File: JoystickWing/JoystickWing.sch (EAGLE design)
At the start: 19 parts, among them J1 5747844-4

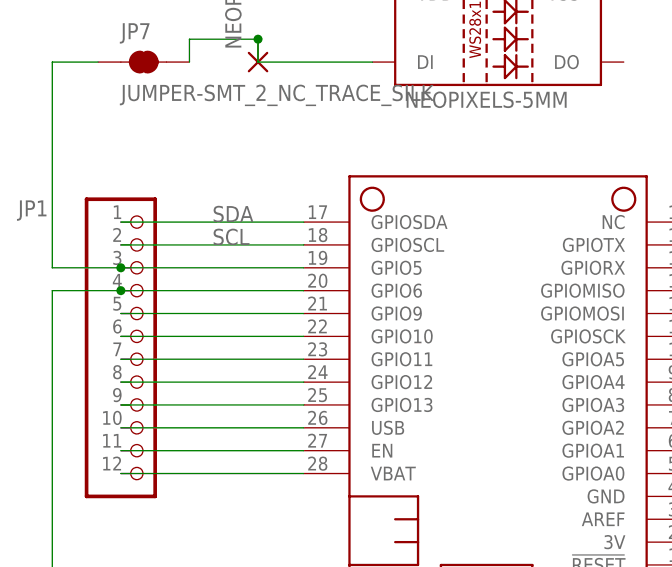
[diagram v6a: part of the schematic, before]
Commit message: Updated to fix errors and sent to PCBWay
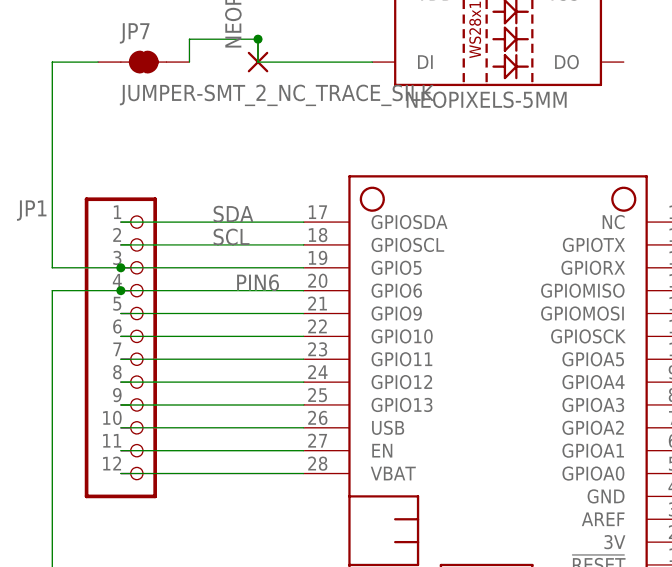
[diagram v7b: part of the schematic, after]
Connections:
- net N$2 renamed PIN6
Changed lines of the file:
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@@
 <grid distance="0.1" unitdist="inch" unit="inch" style="lines" multiple="1" display="no" altdistance="0.01" altunitdist="inch" altunit="inch"/>
 <layers>
-<layer number="1" name="Top" color="4" fill="1" visible="yes" active="no"/>
-<layer number="2" name="Route2" color="1" fill="3" visible="yes" active="no"/>
-<layer number="3" name="Route3" color="4" fill="3" visible="yes" active="no"/>
-<layer number="4" name="Route4" color="1" fill="4" visible="yes" active="no"/>
-<layer number="5" name="Route5" color="4" fill="4" visible="yes" active="no"/>
-<layer number="6" name="Route6" color="1" fill="8" visible="yes" active="no"/>
-<layer number="7" name="Route7" color="4" fill="8" visible="yes" active="no"/>
-<layer number="8" name="Route8" color="1" fill="2" visible="yes" active="no"/>
-<layer number="9" name="Route9" color="4" fill="2" visible="yes" active="no"/>
-<layer number="10" name="Route10" color="1" fill="7" visible="yes" active="no"/>
-<layer number="11" name="Route11" color="4" fill="7" visible="yes" active="no"/>
-<layer number="12" name="Route12" color="1" fill="5" visible="yes" active="no"/>
-<layer number="13" name="Route13" color="4" fill="5" visible="yes" active="no"/>
-<layer number="14" name="Route14" color="1" fill="6" visible="yes" active="no"/>
-<layer number="15" name="Route15" color="4" fill="6" visible="yes" active="no"/>
-<layer number="16" name="Bottom" color="1" fill="1" visible="yes" active="no"/>
-<layer number="17" name="Pads" color="2" fill="1" visible="yes" active="no"/>
-<layer number="18" name="Vias" color="2" fill="1" visible="yes" active="no"/>
-<layer number="19" name="Unrouted" color="6" fill="1" visible="yes" active="no"/>
-<layer number="20" name="Dimension" color="24" fill="1" visible="yes" active="no"/>
-<layer number="21" name="tPlace" color="7" fill="1" visible="yes" active="no"/>
-<layer number="22" name="bPlace" color="7" fill="1" visible="yes" active="no"/>
-<layer number="23" name="tOrigins" color="15" fill="1" visible="yes" active="no"/>
-<layer number="24" name="bOrigins" color="15" fill="1" visible="yes" active="no"/>
-<layer number="25" name="tNames" color="7" fill="1" visible="yes" active="no"/>
-<layer number="26" name="bNames" color="7" fill="1" visible="yes" active="no"/>
-<layer number="27" name="tValues" color="7" fill="1" visible="yes" active="no"/>
-<layer number="28" name="bValues" color="7" fill="1" visible="yes" active="no"/>
+<layer number="1" name="Top" color="4" fill="1" visible="no" active="no"/>
+<layer number="2" name="Route2" color="1" fill="3" visible="no" active="no"/>
+<layer number="3" name="Route3" color="4" fill="3" visible="no" active="no"/>
+<layer number="4" name="Route4" color="1" fill="4" visible="no" active="no"/>
+<layer number="5" name="Route5" color="4" fill="4" visible="no" active="no"/>
+<layer number="6" name="Route6" color="1" fill="8" visible="no" active="no"/>
+<layer number="7" name="Route7" color="4" fill="8" visible="no" active="no"/>
+<layer number="8" name="Route8" color="1" fill="2" visible="no" active="no"/>
+<layer number="9" name="Route9" color="4" fill="2" visible="no" active="no"/>
+<layer number="10" name="Route10" color="1" fill="7" visible="no" active="no"/>
+<layer number="11" name="Route11" color="4" fill="7" visible="no" active="no"/>
+<layer number="12" name="Route12" color="1" fill="5" visible="no" active="no"/>
+<layer number="13" name="Route13" color="4" fill="5" visible="no" active="no"/>
+<layer number="14" name="Route14" color="1" fill="6" visible="no" active="no"/>
+<layer number="15" name="Route15" color="4" fill="6" visible="no" active="no"/>
+<layer number="16" name="Bottom" color="1" fill="1" visible="no" active="no"/>
+<layer number="17" name="Pads" color="2" fill="1" visible="no" active="no"/>
+<layer number="18" name="Vias" color="2" fill="1" visible="no" active="no"/>
+<layer number="19" name="Unrouted" color="6" fill="1" visible="no" active="no"/>
+<layer number="20" name="Dimension" color="24" fill="1" visible="no" active="no"/>
+<layer number="21" name="tPlace" color="7" fill="1" visible="no" active="no"/>
+<layer number="22" name="bPlace" color="7" fill="1" visible="no" active="no"/>
+<layer number="23" name="tOrigins" color="15" fill="1" visible="no" active="no"/>
+<layer number="24" name="bOrigins" color="15" fill="1" visible="no" active="no"/>
+<layer number="25" name="tNames" color="7" fill="1" visible="no" active="no"/>
+<layer number="26" name="bNames" color="7" fill="1" visible="no" active="no"/>
+<layer number="27" name="tValues" color="7" fill="1" visible="no" active="no"/>
+<layer number="28" name="bValues" color="7" fill="1" visible="no" active="no"/>
 <layer number="29" name="tStop" color="7" fill="3" visible="no" active="no"/>
 <layer number="30" name="bStop" color="7" fill="6" visible="no" active="no"/>
@@
 <layer number="35" name="tGlue" color="7" fill="4" visible="no" active="no"/>
 <layer number="36" name="bGlue" color="7" fill="5" visible="no" active="no"/>
-<layer number="37" name="tTest" color="7" fill="1" visible="yes" active="no"/>
-<layer number="38" name="bTest" color="7" fill="1" visible="yes" active="no"/>
+<layer number="37" name="tTest" color="7" fill="1" visible="no" active="no"/>
+<layer number="38" name="bTest" color="7" fill="1" visible="no" active="no"/>
 <layer number="39" name="tKeepout" color="4" fill="11" visible="no" active="no"/>
 <layer number="40" name="bKeepout" color="1" fill="11" visible="no" active="no"/>
@@
 <layer number="44" name="Drills" color="7" fill="1" visible="no" active="no"/>
 <layer number="45" name="Holes" color="7" fill="1" visible="no" active="no"/>
-<layer number="46" name="Milling" color="3" fill="1" visible="yes" active="no"/>
-<layer number="47" name="Measures" color="7" fill="1" visible="yes" active="no"/>
-<layer number="48" name="Document" color="7" fill="1" visible="yes" active="no"/>
-<layer number="49" name="Reference" color="7" fill="1" visible="yes" active="no"/>
-<layer number="50" name="dxf" color="7" fill="1" visible="yes" active="no"/>
-<layer number="51" name="tDocu" color="7" fill="1" visible="yes" active="no"/>
-<layer number="52" name="bDocu" color="7" fill="1" visible="yes" active="no"/>
-<layer number="53" name="tGND_GNDA" color="7" fill="9" visible="yes" active="no"/>
-<layer number="54" name="bGND_GNDA" color="1" fill="9" visible="yes" active="no"/>
-<layer number="56" name="wert" color="7" fill="1" visible="yes" active="no"/>
-<layer number="57" name="tCAD" color="7" fill="1" visible="yes" active="no"/>
-<layer number="58" name="bCAD" color="7" fill="1" visible="yes" active="no"/>
-<layer number="59" name="tCarbon" color="7" fill="1" visible="yes" active="no"/>
-<layer number="60" name="bCarbon" color="7" fill="1" visible="yes" active="no"/>
-<layer number="61" name="stand" color="7" fill="1" visible="yes" active="no"/>
+<layer number="46" name="Milling" color="3" fill="1" visible="no" active="no"/>
+<layer number="47" name="Measures" color="7" fill="1" visible="no" active="no"/>
+<layer number="48" name="Document" color="7" fill="1" visible="no" active="no"/>
+<layer number="49" name="Reference" color="7" fill="1" visible="no" active="no"/>
+<layer number="50" name="dxf" color="7" fill="1" visible="no" active="no"/>
+<layer number="51" name="tDocu" color="7" fill="1" visible="no" active="no"/>
+<layer number="52" name="bDocu" color="7" fill="1" visible="no" active="no"/>
+<layer number="53" name="tGND_GNDA" color="7" fill="9" visible="no" active="no"/>
+<layer number="54" name="bGND_GNDA" color="1" fill="9" visible="no" active="no"/>
+<layer number="56" name="wert" color="7" fill="1" visible="no" active="no"/>
+<layer number="57" name="tCAD" color="7" fill="1" visible="no" active="no"/>
+<layer number="58" name="bCAD" color="7" fill="1" visible="no" active="no"/>
+<layer number="59" name="tCarbon" color="7" fill="1" visible="no" active="no"/>
+<layer number="60" name="bCarbon" color="7" fill="1" visible="no" active="no"/>
+<layer number="61" name="stand" color="7" fill="1" visible="no" active="no"/>
 <layer number="88" name="SimResults" color="9" fill="1" visible="yes" active="yes"/>
 <layer number="89" name="SimProbes" color="9" fill="1" visible="yes" active="yes"/>
@@
 </segment>
 </net>
-<net name="N$2" class="0">
+<net name="PIN6" class="0">
 <segment>
 <pinref part="MS1" gate="G$1" pin="GPIO6"/>
@@
 <wire x1="-127" y1="60.96" x2="-119.38" y2="60.96" width="0.1524" layer="91"/>
 <junction x="-119.38" y="60.96"/>
-</segment>
-</net>
+<label x="-106.68" y="60.96" size="1.778" layer="95"/>
+</segment>
+</net>

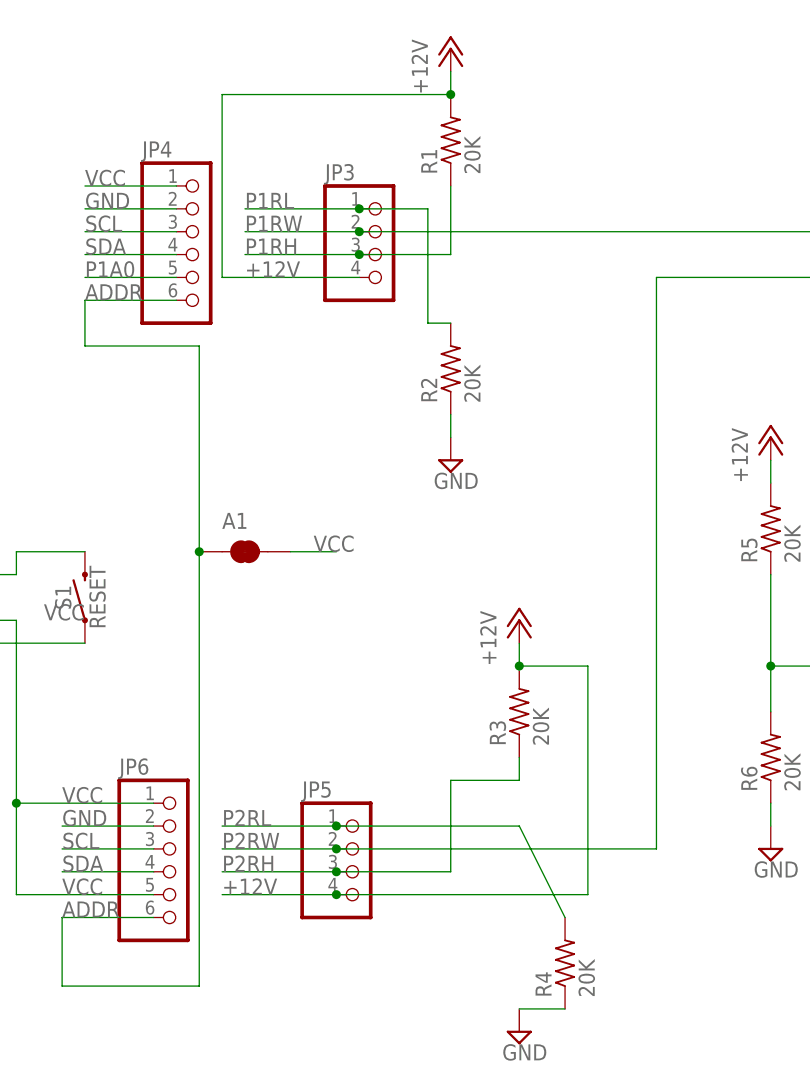
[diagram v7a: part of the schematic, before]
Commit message: Removed bad V+ connection and cleaned up
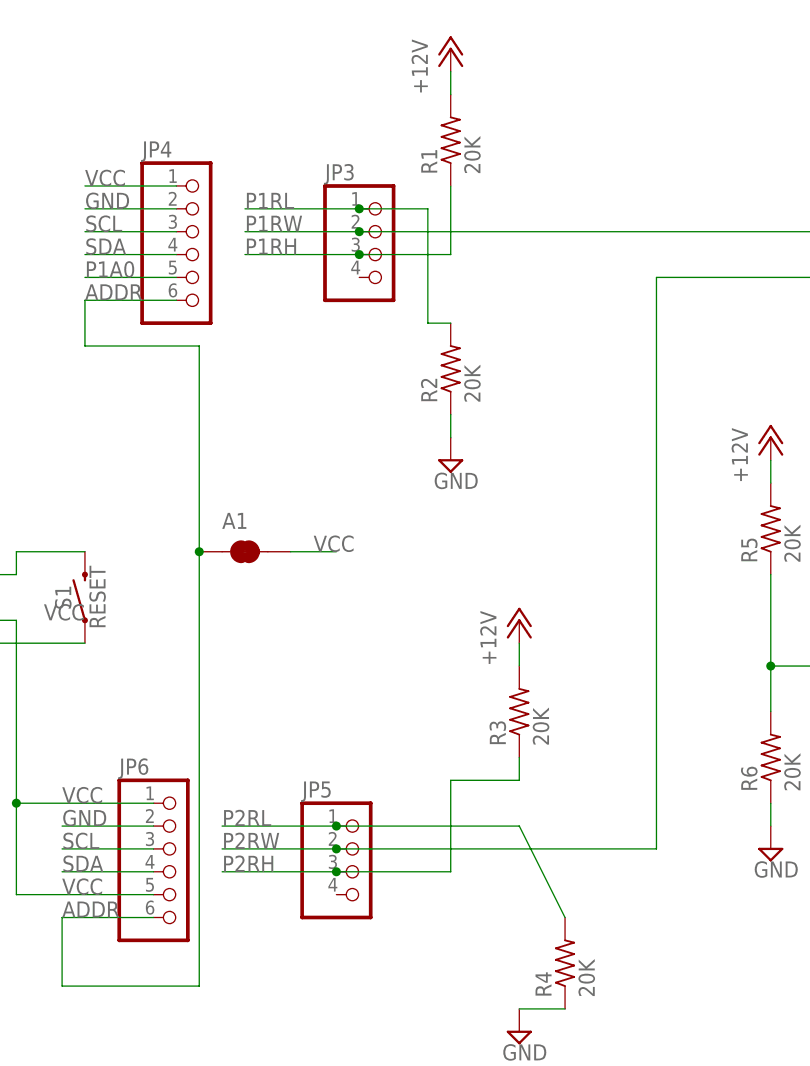
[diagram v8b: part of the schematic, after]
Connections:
- net +12V: no longer JP3.4, JP5.4
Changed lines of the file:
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@@
 <?xml version="1.0" encoding="utf-8"?>
 <!DOCTYPE eagle SYSTEM "eagle.dtd">
-<eagle version="9.2.2">
+<eagle version="9.6.2">
 <drawing>
 <settings>
@@
 <pinref part="R3" gate="G$1" pin="2"/>
 <wire x1="25.4" y1="30.48" x2="25.4" y2="27.94" width="0.1524" layer="91"/>
-<pinref part="JP5" gate="A" pin="4"/>
-<wire x1="5.08" y1="2.54" x2="-7.62" y2="2.54" width="0.1524" layer="91"/>
-<label x="-7.62" y="2.54" size="1.778" layer="95"/>
-<wire x1="5.08" y1="2.54" x2="33.02" y2="2.54" width="0.1524" layer="91"/>
-<junction x="5.08" y="2.54"/>
-<wire x1="33.02" y1="2.54" x2="33.02" y2="27.94" width="0.1524" layer="91"/>
-<wire x1="33.02" y1="27.94" x2="25.4" y2="27.94" width="0.1524" layer="91"/>
-<junction x="25.4" y="27.94"/>
 </segment>
 <segment>
@@
 <pinref part="P+1" gate="1" pin="+12V"/>
 <wire x1="17.78" y1="91.44" x2="17.78" y2="93.98" width="0.1524" layer="91"/>
-<pinref part="JP3" gate="A" pin="4"/>
-<wire x1="7.62" y1="71.12" x2="-7.62" y2="71.12" width="0.1524" layer="91"/>
-<label x="-5.08" y="71.12" size="1.778" layer="95"/>
-<wire x1="-7.62" y1="71.12" x2="-7.62" y2="91.44" width="0.1524" layer="91"/>
-<wire x1="-7.62" y1="91.44" x2="17.78" y2="91.44" width="0.1524" layer="91"/>
-<junction x="17.78" y="91.44"/>
 </segment>
 </net>
